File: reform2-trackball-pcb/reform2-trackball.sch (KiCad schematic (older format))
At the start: 42 parts, among them J1 Conn_USB, J2 Conn_01x06_Female, SW1 Choc, SW2 Choc, SW3 Choc, SW4 Choc, SW5 Choc, SW6 SW_RST, SW7 SW_HWB, U1 ATmega32U2-AU, U2 TLV75533PDBV, Y1 Crystal_GND24

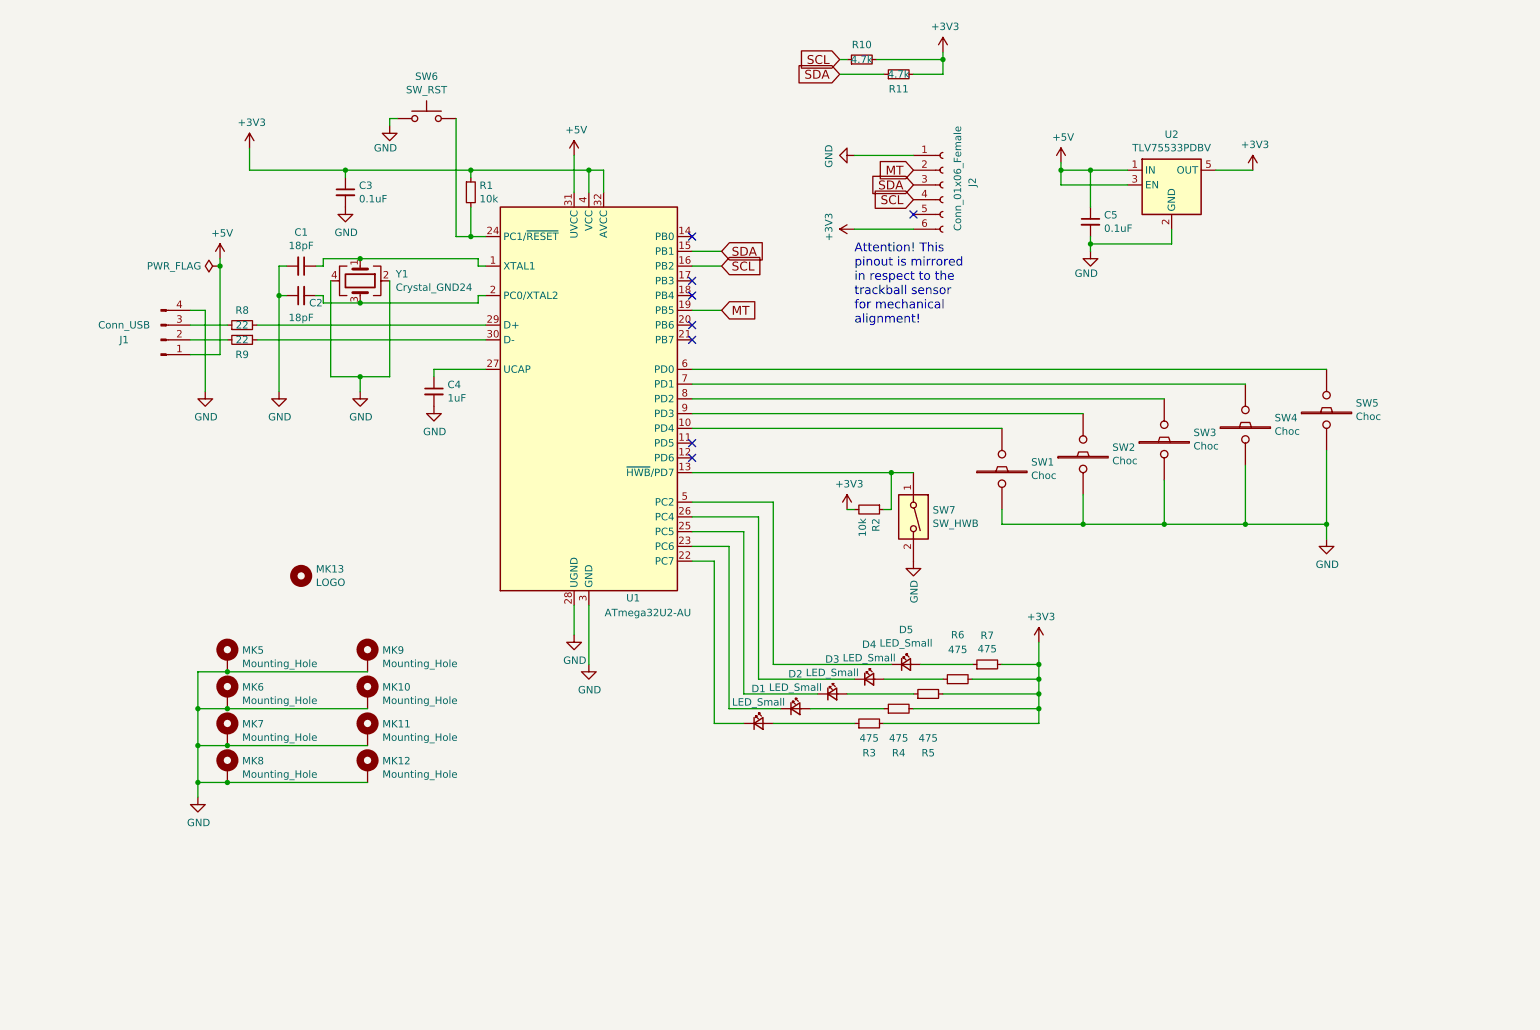
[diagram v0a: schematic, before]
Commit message: trackball-pcb: R-1 version with ESD protection and fuse
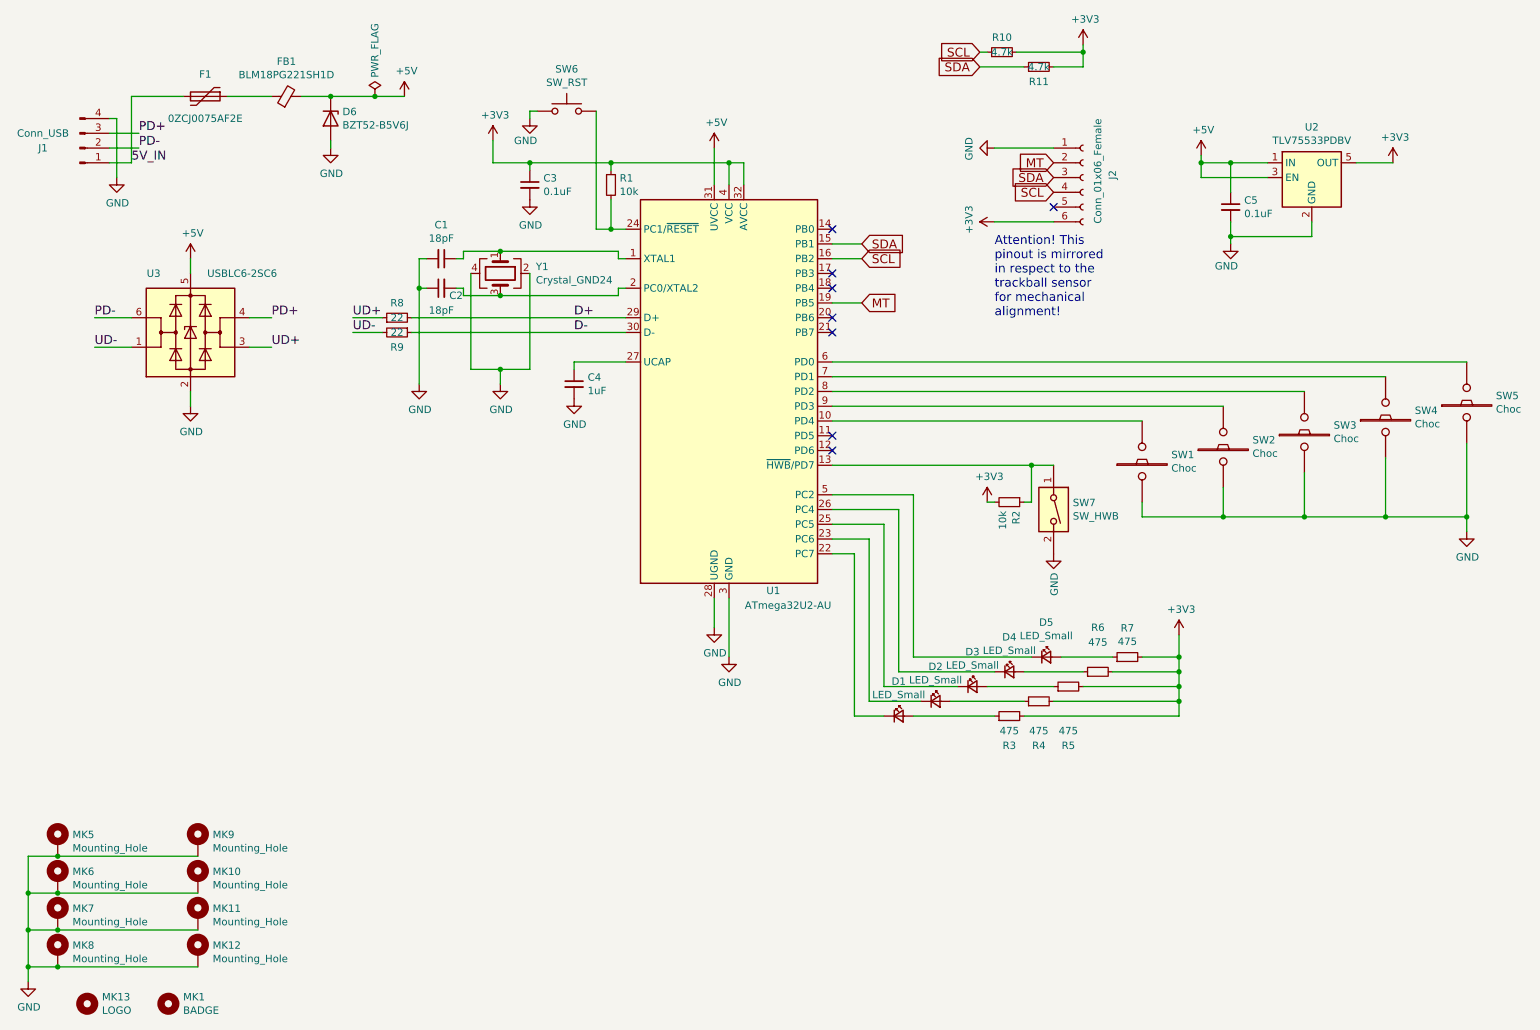
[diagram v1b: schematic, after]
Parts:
- added D6: BZT52-B5V6J, Diode_SMD:D_SOD-123, symbol Diode:BZT52Bxx
- added F1: 0ZCJ0075AF2E, Fuse:Fuse_1206_3216Metric_Castellated, symbol Device:Polyfuse
- added FB1: BLM18PG221SH1D, Inductor_SMD:L_0603_1608Metric, symbol Device:Ferrite_Bead_Small
- added MK1: BADGE, footprints-trackball:mntreform-trackball-badge, symbol Mechanical:MountingHole
- added U3: USBLC6-2SC6, Package_TO_SOT_SMD:SOT-23-6, symbol Power_Protection:USBLC6-2SC6
- Y1: footprint Crystals:Crystal_SMD_3225-4pin_3.2x2.5mm_HandSoldering -> Crystal:Crystal_SMD_3225-4Pin_3.2x2.5mm
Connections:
- net +5V: now also D6.1 (K), FB1.2, U3.5 (VBUS); no longer J1.1 (Pin_1)
- net GND: now also D6.2 (A), U3.2 (GND)
- net D+: now reaches R8.2, U1.29 (D+)
- net D-: now reaches R9.1, U1.30 (D-)
- net PD-: now reaches J1.2 (Pin_2)
- net PD-: now also U3.6 (I/O1); no longer R9.2
- net PD+: now reaches J1.3 (Pin_3)
- net PD+: now also U3.4 (I/O2); no longer R8.1
- new net: F1.1, FB1.1
- new net 5V_IN: F1.2, J1.1 (Pin_1)
- new net UD+: R8.1, U3.3 (I/O2)
- new net UD-: R9.2, U3.1 (I/O1)
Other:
- moved on the sheet: C1, C2, C3, C4, C5, D1, D2, D3, D4, D5, J1, J2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
